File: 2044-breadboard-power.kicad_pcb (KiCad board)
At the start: 2 copper layers, 51 x 22 mm, 13 parts, among them J1 Conn_02x02_Odd_Even, J2 PJ-102AH, J3 Conn_02x02_Odd_Even, U1 AZ1117CH-3.3TRG1, U2 AZ1117CH-5.0TRG1

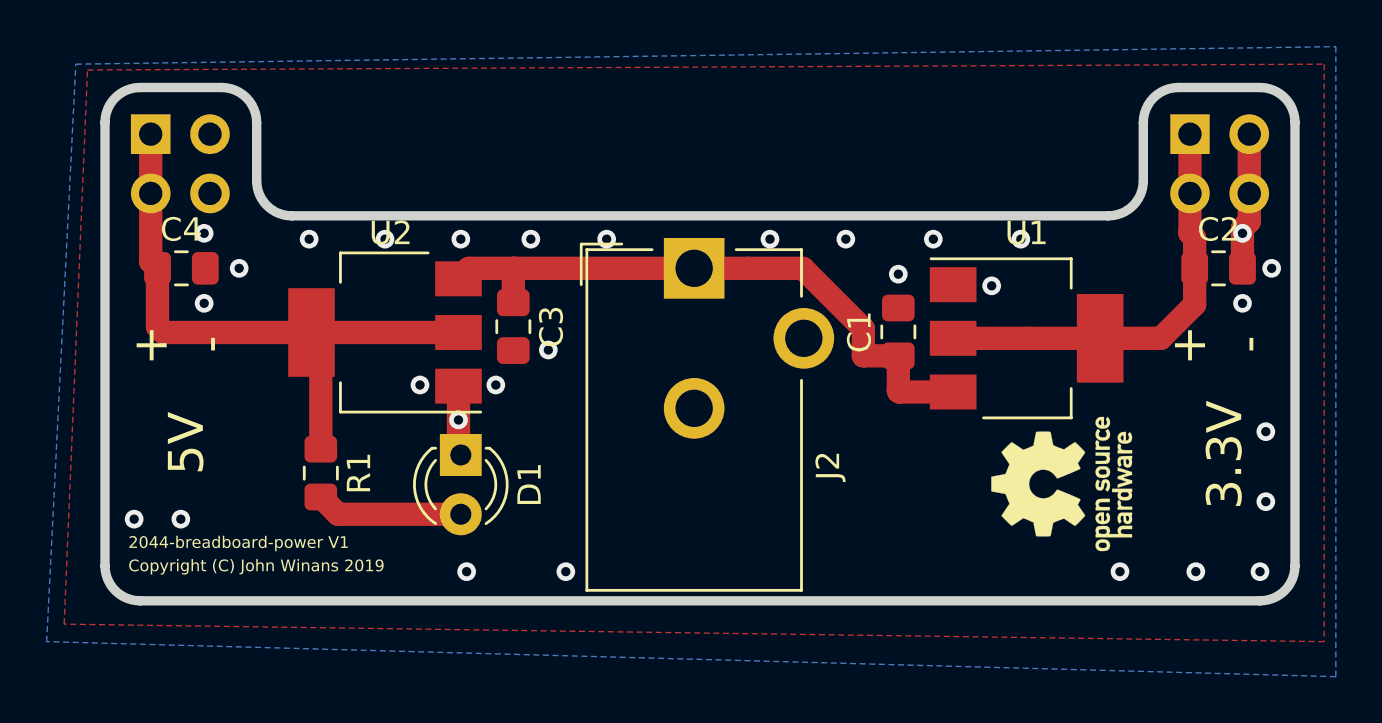
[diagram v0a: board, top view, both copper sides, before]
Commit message: Change power connector to USB & remove 5V reg.
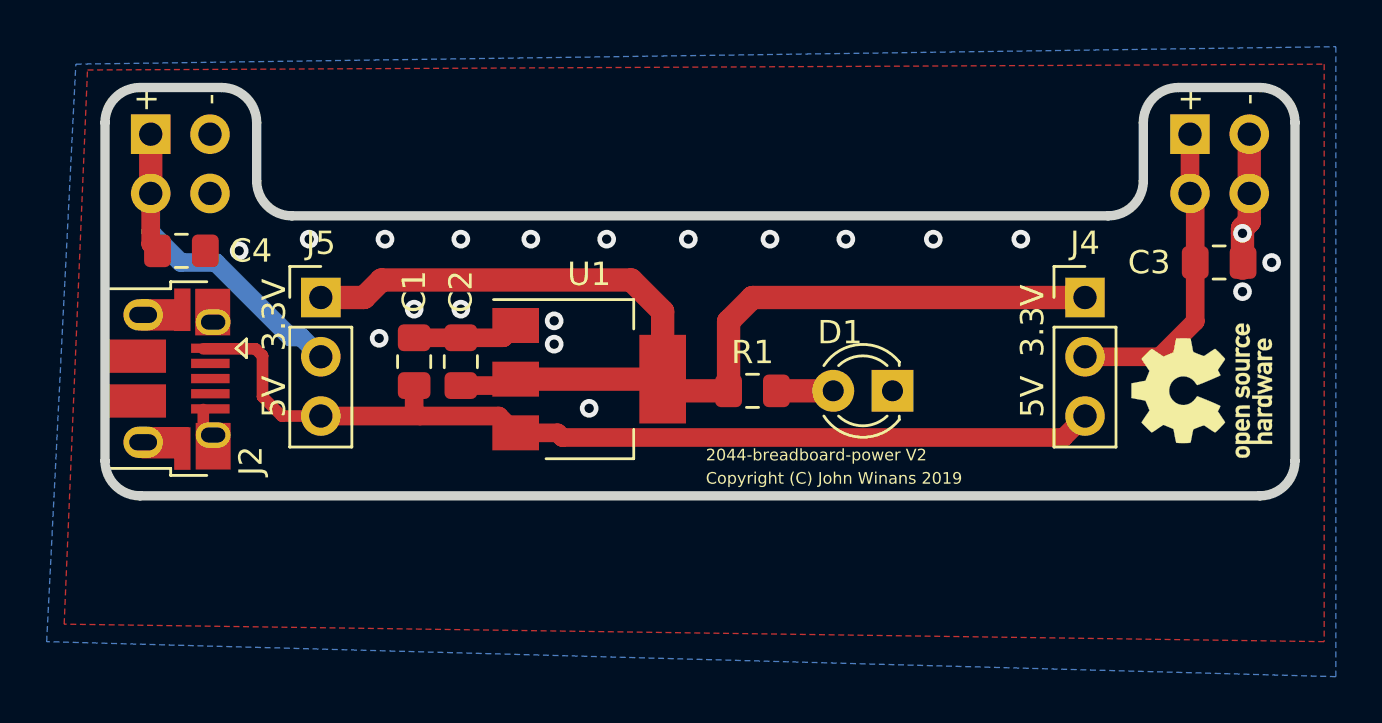
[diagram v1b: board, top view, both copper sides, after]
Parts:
- removed U2: AZ1117CH-5.0TRG1, Package_TO_SOT_SMD:SOT-223-3_TabPin2
- added J4: Conn_01x03, Connector_PinHeader_2.54mm:PinHeader_1x03_P2.54mm_Vertical, F.Cu at (157.5, 70.0)
- added J5: Conn_01x03, Connector_PinHeader_2.54mm:PinHeader_1x03_P2.54mm_Vertical, F.Cu at (124.8, 70.0)
- C3: value 10uF -> 22uF
- J2: value PJ-102AH -> USB_B_Micro; footprint Connector_BarrelJack:BarrelJack_CUI_PJ-102AH_Horizontal -> Connector_USB:USB_Micro-B_Amphenol_10103594-0001LF_Horizontal
- moved C2 32.7 mm to (130.8, 72.8), turned to 90 degrees
- moved C3 30.4 mm to (163.2, 68.5), turned to 0 degrees
- moved J2 23.0 mm to (118.2, 73.5), turned to 270 degrees
- moved C1 20.8 mm to (128.8, 72.8)
- moved R1 18.8 mm to (143.2, 74.0), turned to 0 degrees
- moved U1 18.8 mm to (136.2, 73.5)
- moved D1 18.7 mm to (149.2, 74.0), turned to 180 degrees
- moved REF** 7.21 mm to (162.5, 74.0)
- moved REF** 2.76 mm to (162.2, 72.5)
- moved C4 0.75 mm to (118.8, 68.0)
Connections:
- C1 pad 1: Net-(C1-Pad1) -> +5V
- C2 pad 1: Net-(C2-Pad1) -> +3V3
- C3 pad 1: Net-(C1-Pad1) -> /Vout1
- C4 pad 1: Net-(C4-Pad1) -> /Vout2
- J1 pad 1: Net-(C2-Pad1) -> /Vout1
- J1 pad 2: Net-(C2-Pad1) -> /Vout1
- J2 pad 1: Net-(C1-Pad1) -> +5V
- J2 pad 2: GND -> Net-(J2-Pad2)
- J2 pad 3: (no net) -> Net-(J2-Pad3)
- J3 pad 1: Net-(C4-Pad1) -> /Vout2
- J3 pad 2: Net-(C4-Pad1) -> /Vout2
- R1 pad 1: Net-(C4-Pad1) -> +3V3
- U1 pad 2: Net-(C2-Pad1) -> +3V3
- U1 pad 3: Net-(C1-Pad1) -> +5V
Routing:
- net +3V3: track 0.00 -> 48.9 mm
- net +5V: track 0.00 -> 41.8 mm
- net Net-(C1-Pad1): track 26.6 -> 0.00 mm
- net Net-(C4-Pad1): track 26.5 -> 0.00 mm
- net Net-(C2-Pad1): track 18.3 -> 0.00 mm
- net /Vout2: track 0.00 -> 16.3 mm
- net /Vout1: track 0.00 -> 13.5 mm
- net Net-(D1-Pad2): track 6.31 -> 2.44 mm
- net GND: track 8.86 -> 11.6 mm, vias 30 -> 20
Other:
- board size 51 x 22 mm -> 51 x 17.5 mm
- board text added: "2044-breadboard-power V2"
- board text removed: "2044-breadboard-power V1"

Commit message: Fix typo in solder mask width value.
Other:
- rule solder_mask_min_width: 0.25 -> 0.1016
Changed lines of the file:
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@@
     (pad_drill 0.762)
     (pad_to_mask_clearance 0.0762)
-    (solder_mask_min_width 0.25)
+    (solder_mask_min_width 0.1016)
     (aux_axis_origin 0 0)
     (visible_elements FFFFFF7F)
